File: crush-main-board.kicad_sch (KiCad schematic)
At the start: 25 parts, among them J1 4x4_Header, J10 3x3 Header, J11 3x3 Header, J12 3x2 Header, J13 3x4_Header, J14 3x4_Header, J15 2157601008, J2 4x4_Header, J3 6x2_Header, J4 3x1_Header, J5 3x2 Header, J6 3x2 Header, J7 3x4 Header, J8 3x4 Header, J9 3x3 Header, U1 Teensy4.1, U2 ISO7740DW, U3 ISO7740DW

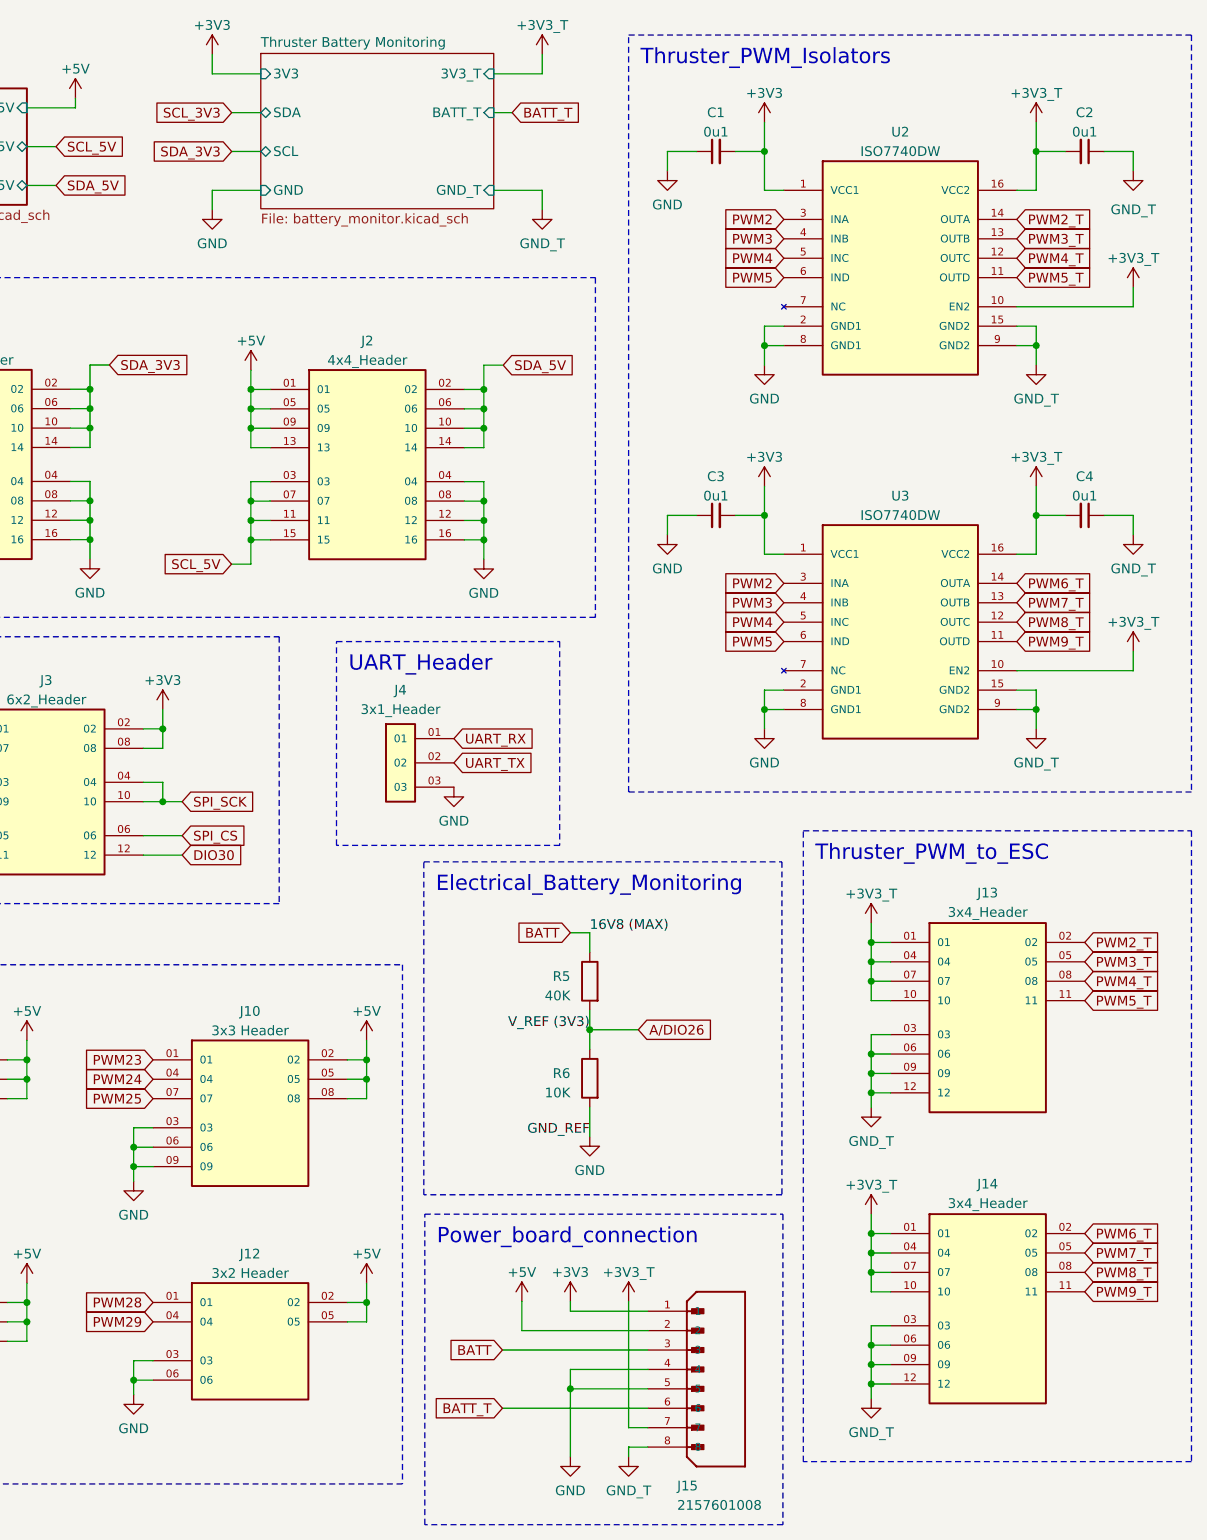
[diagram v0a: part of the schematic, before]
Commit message: Fixed an error of the "3V3_T" and "GND_T" and added some conditions for the PCB design
The power nets for the thruster side require their own custom symbols unless they will refer to the same ones that are linked to the normal power nets
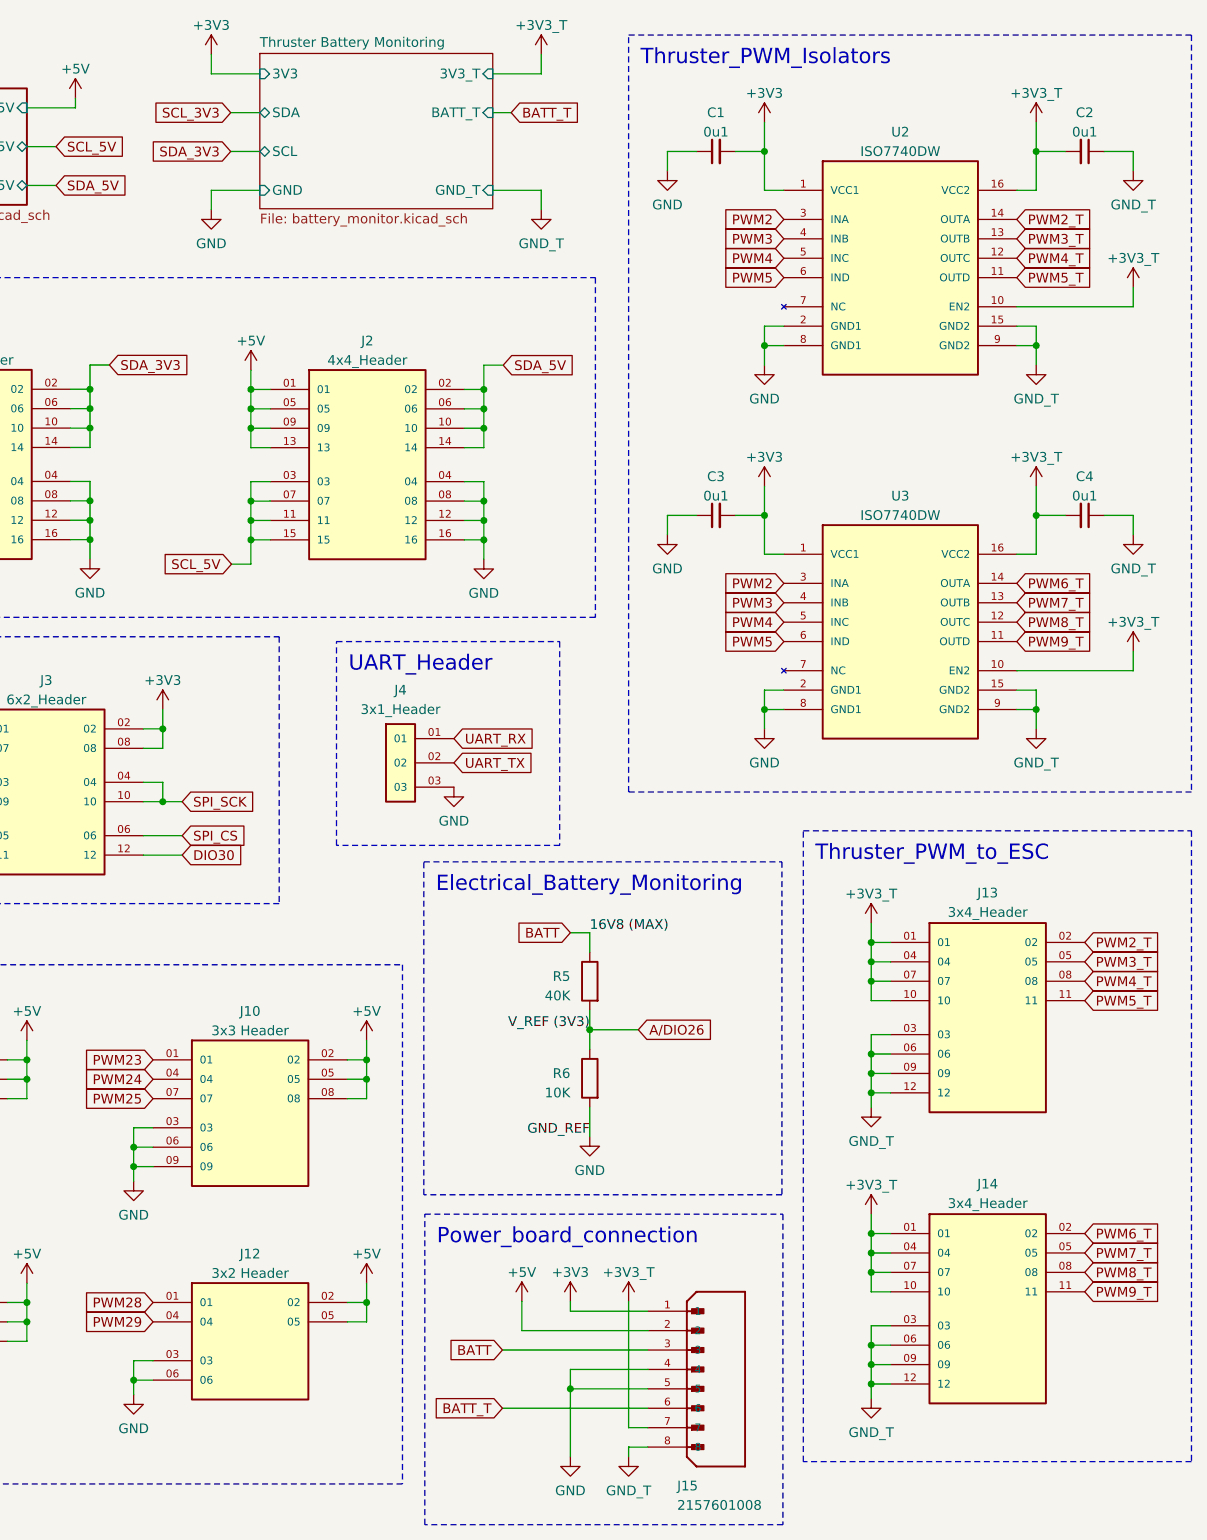
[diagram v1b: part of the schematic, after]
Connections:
- net +3V3: now also J15.1; no longer C4.2, J13.01, J13.04, J13.07, J13.10, J14.01, J14.04, J14.07, J14.10, J15.7, U2.10 (EN2), U3.10 (EN2), U3.16 (VCC2)
- net +5V: no longer J15.1
- net GND: no longer C2.1, C4.1, J13.03, J13.06, J13.09, J13.12, J14.03, J14.06, J14.09, J14.12, J15.8, U2.15 (GND2), U2.9 (GND2), U3.15 (GND2), U3.9 (GND2)
- new net +3V3_T: C4.2, J13.01, J13.04, J13.07, J13.10, J14.01, J14.04, J14.07, J14.10, J15.7, U2.10 (EN2), U3.10 (EN2), U3.16 (VCC2)
- new net GND_T: C2.1, C4.1, J13.03, J13.06, J13.09, J13.12, J14.03, J14.06, J14.09, J14.12, J15.8, U2.15 (GND2), U2.9 (GND2), U3.15 (GND2), U3.9 (GND2)

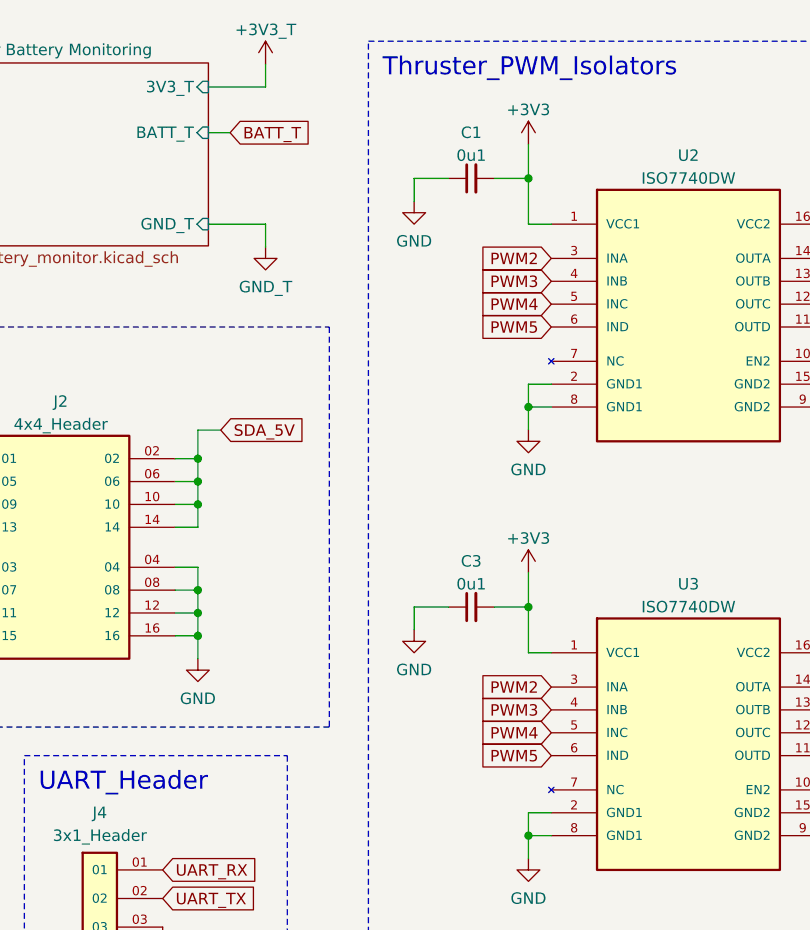
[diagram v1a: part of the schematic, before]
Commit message: Fixed some minor errors and arranged the components into two ground sides
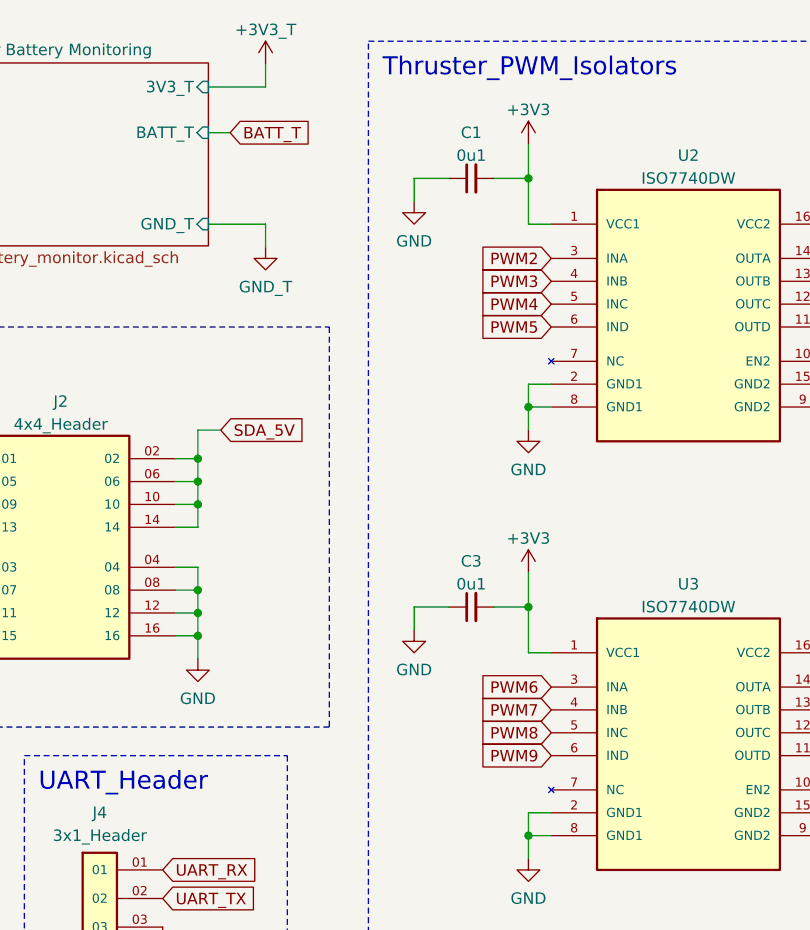
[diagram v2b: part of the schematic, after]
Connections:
- net PWM2: no longer U3.3 (INA)
- net PWM3: no longer U3.4 (INB)
- net PWM4: no longer U3.5 (INC)
- net PWM5: no longer U3.6 (IND)
- net PWM6: now also U3.3 (INA)
- net PWM7: now also U3.4 (INB)
- net PWM8: now also U3.5 (INC)
- net PWM9: now also U3.6 (IND)

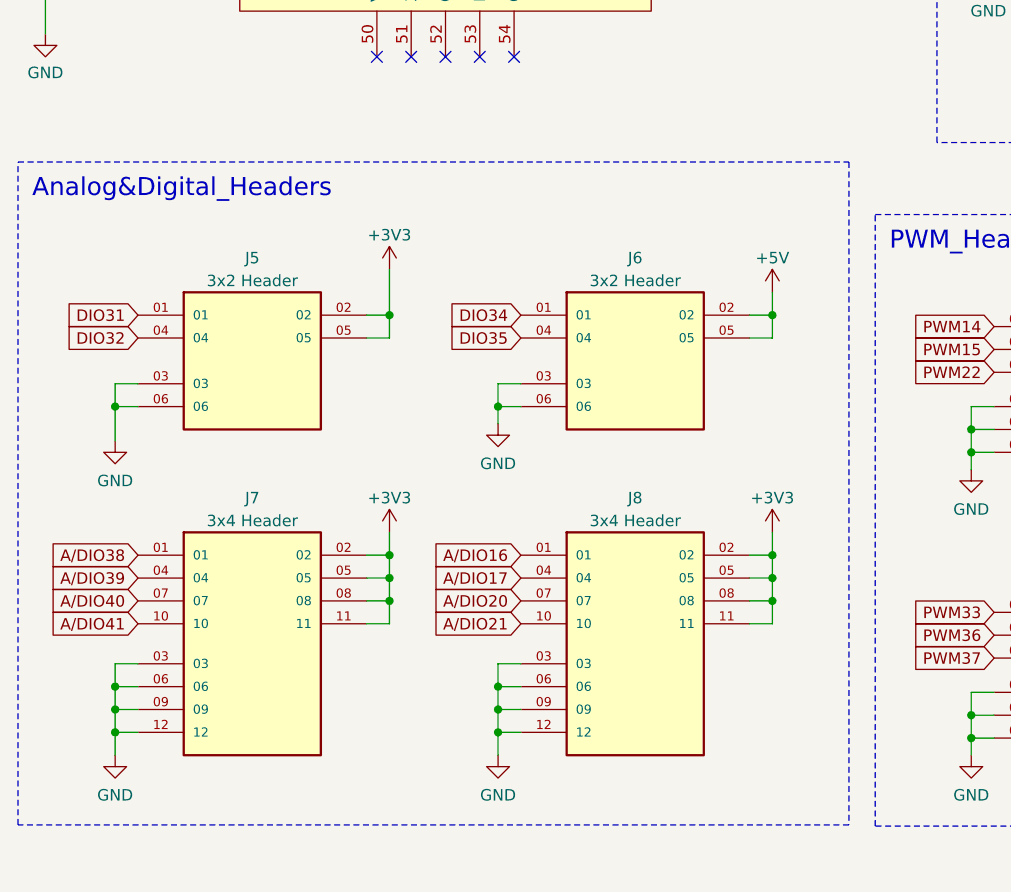
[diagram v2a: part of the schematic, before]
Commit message: re-aligned the elements based on their grounds
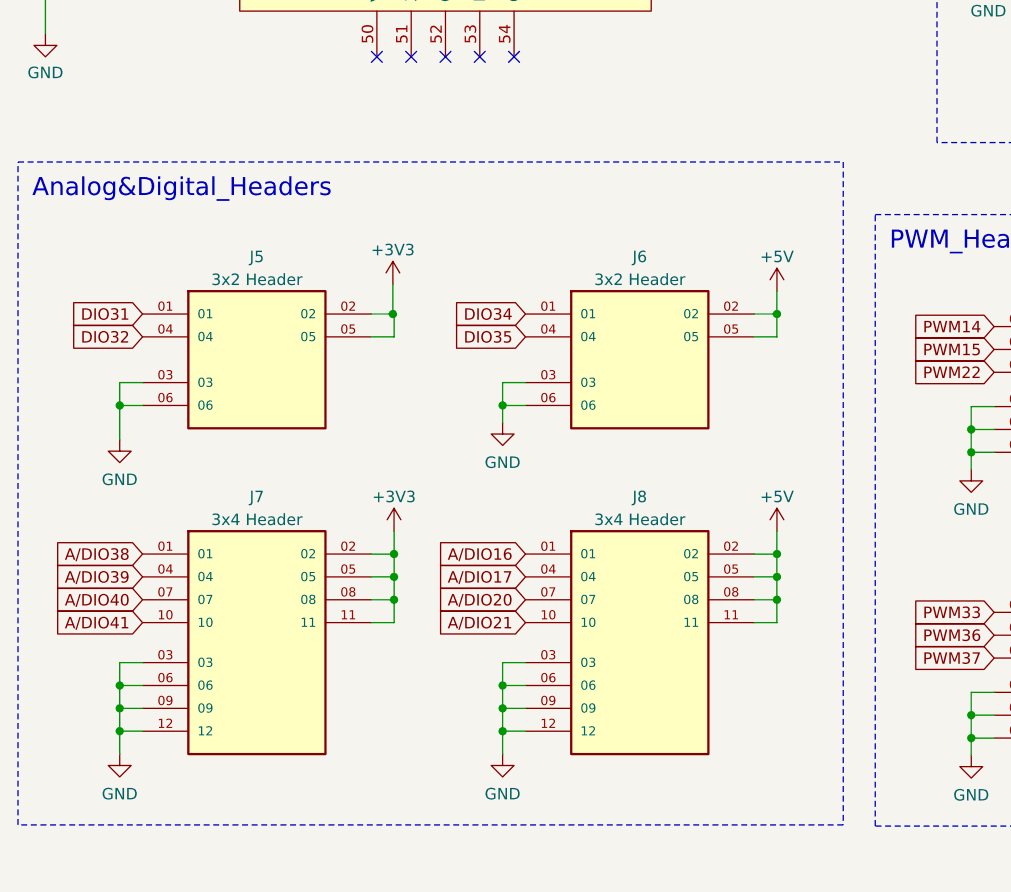
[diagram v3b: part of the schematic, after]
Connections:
- net +3V3: now also J1.01, J1.05, J1.09, J1.13; no longer J8.02, J8.05, J8.08, J8.11
- net +5V: now also J8.02, J8.05, J8.08, J8.11; no longer J1.01, J1.05, J1.09, J1.13
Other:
- moved on the sheet: J5, J6, J7, J8

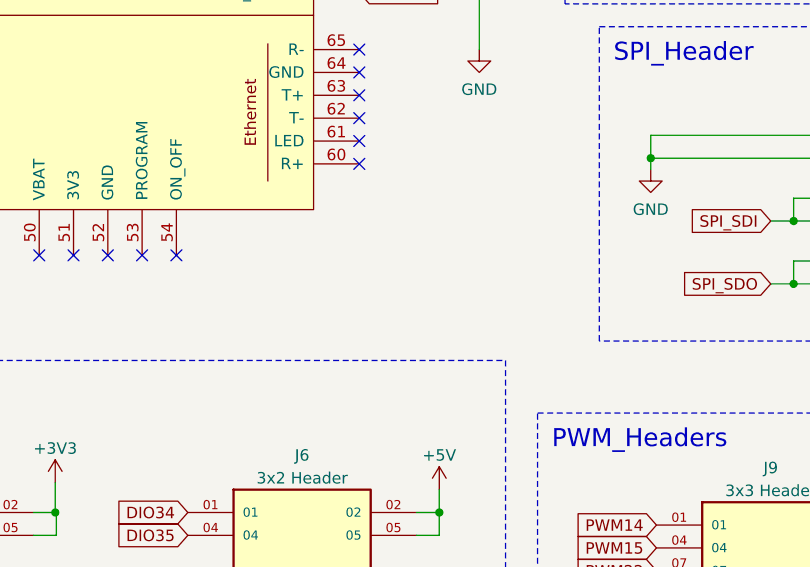
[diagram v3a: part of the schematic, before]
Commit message: Sketch out a possible circuit for the killswitch
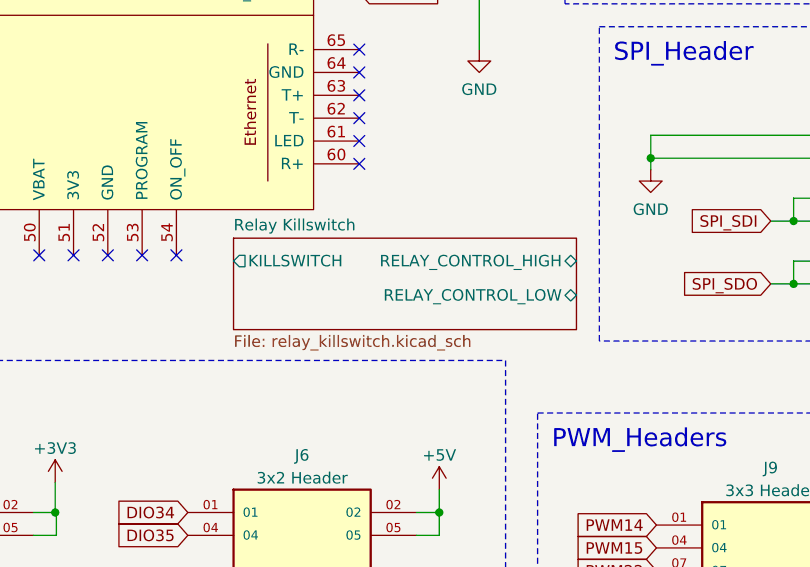
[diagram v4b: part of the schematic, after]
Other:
- added sheet Relay Killswitch (relay_killswitch.kicad_sch)
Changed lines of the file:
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@@
+    )
+  )
+  (sheet (at 64.77 109.22) (size 38.1 10.16) (fields_autoplaced)
+    (stroke (width 0.1524) (type solid))
+    (fill (color 0 0 0 0.0000))
+    (property "Sheetname" "Relay Killswitch" (at 64.77 108.5084 0)
+      (effects (font (size 1.27 1.27)) (justify left bottom))
+    )
+    (property "Sheetfile" "relay_killswitch.kicad_sch" (at 64.77 119.9646 0)
+      (effects (font (size 1.27 1.27)) (justify left top))
+    )
+    (pin "KILLSWITCH" output (at 64.77 111.76 180)
+      (effects (font (size 1.27 1.27)) (justify left))
+    )
+    (pin "RELAY_CONTROL_HIGH" bidirectional (at 102.87 111.76 0)
+      (effects (font (size 1.27 1.27)) (justify right))
+    )
+    (pin "RELAY_CONTROL_LOW" bidirectional (at 102.87 115.57 0)
+      (effects (font (size 1.27 1.27)) (justify right))
+    )
+    (instances
+      (project "crush-main-board"
+        (path "/74b566fe-9d71-4817-95ed-d472d647f8c8" (page "4"))
+      )
     )
   )
